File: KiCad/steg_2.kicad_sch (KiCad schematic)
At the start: 10 parts, among them U12 W65C02S

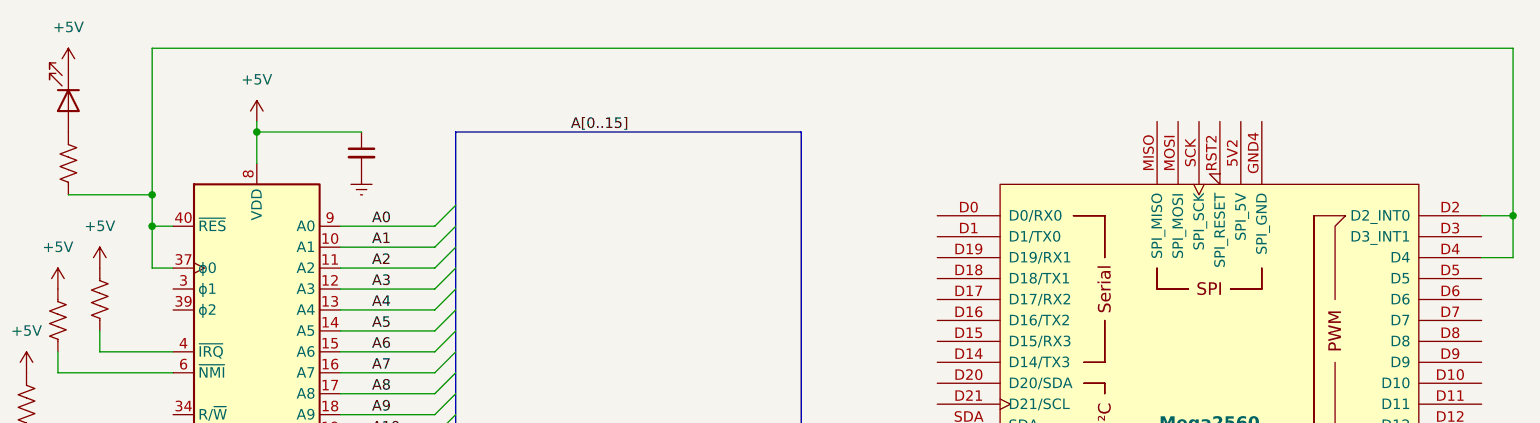
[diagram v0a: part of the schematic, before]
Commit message: Add trim potentiometer symbol and update power symbols in schematics
- Introduced a new trim potentiometer symbol (Device:R_Potentiometer_Trim) with properties for reference, value, footprint, and simulation details.
- Updated existing power symbols for +5V and Earth, including new references and descriptions.
- Adjusted positions and properties of various components in the schematic to enhance clarity and organization.
- Updated multiple schematic images to reflect the latest changes.
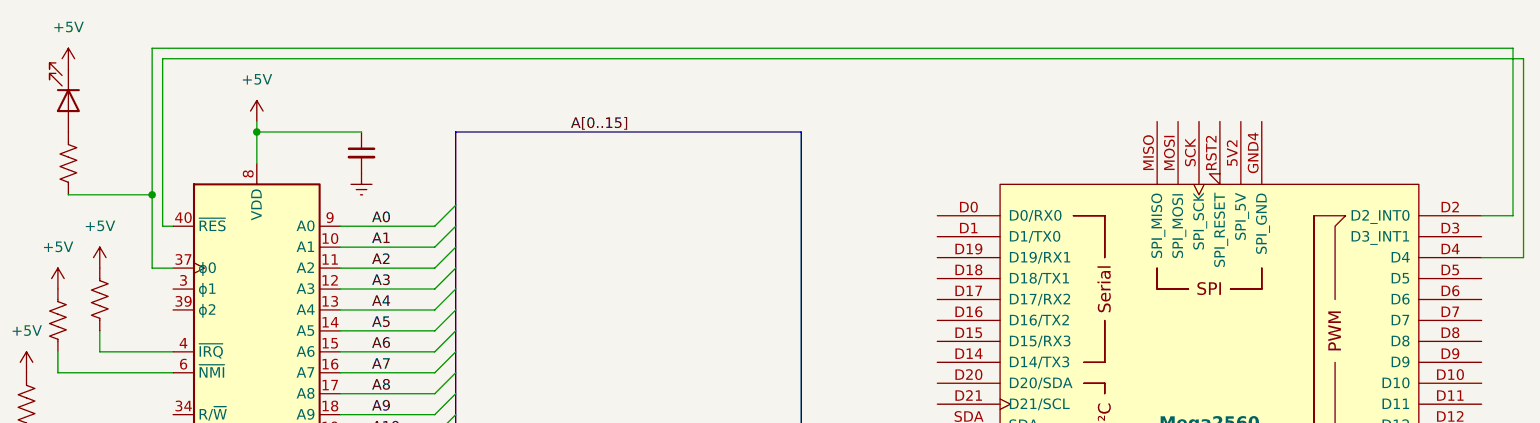
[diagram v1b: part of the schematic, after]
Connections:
- net at A6.D2 (D2_INT0), R34.2, U12.37 (ϕ0): no longer A6.D4, U12.40 (~{RES})
- new net: A6.D4, U12.40 (~{RES})
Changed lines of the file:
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@@
-	)
-	(junction
-		(at 259.08 67.31)
-		(diameter 0)
-		(color 0 0 0 0)
 	)
 	(junction
@@
 		(color 0 0 0 0)
 	)
-	(junction
-		(at 93.98 68.58)
-		(diameter 0)
-		(color 0 0 0 0)
-	)
 	(bus_entry
 		(at 172.72 128.27)
@@
 	(wire
 		(pts
-			(xy 93.98 68.58) (xy 93.98 73.66)
-		)
-		(stroke
-			(width 0)
-			(type default)
-		)
-	)
-	(wire
-		(pts
 			(xy 175.26 128.27) (xy 189.23 128.27)
 		)
@@
 	(wire
 		(pts
-			(xy 259.08 72.39) (xy 255.27 72.39)
-		)
-		(stroke
-			(width 0)
-			(type default)
-		)
-	)
-	(wire
-		(pts
 			(xy 116.84 104.14) (xy 128.27 104.14)
 		)
@@
 	(wire
 		(pts
-			(xy 96.52 68.58) (xy 93.98 68.58)
-		)
-		(stroke
-			(width 0)
-			(type default)
-		)
-	)
-	(wire
-		(pts
 			(xy 116.84 73.66) (xy 128.27 73.66)
 		)
@@
 	(wire
 		(pts
+			(xy 95.25 68.58) (xy 95.25 48.26)
+		)
+		(stroke
+			(width 0)
+			(type default)
+		)
+	)
+	(wire
+		(pts
 			(xy 106.68 57.15) (xy 106.68 60.96)
 		)
@@
 	(wire
 		(pts
-			(xy 93.98 64.77) (xy 93.98 68.58)
+			(xy 93.98 64.77) (xy 93.98 73.66)
 		)
 		(stroke
@@
 	(wire
 		(pts
+			(xy 255.27 72.39) (xy 260.35 72.39)
+		)
+		(stroke
+			(width 0)
+			(type default)
+		)
+	)
+	(wire
+		(pts
 			(xy 93.98 73.66) (xy 96.52 73.66)
 		)
@@
 	(wire
 		(pts
+			(xy 96.52 68.58) (xy 95.25 68.58)
+		)
+		(stroke
+			(width 0)
+			(type default)
+		)
+	)
+	(wire
+		(pts
 			(xy 259.08 46.99) (xy 259.08 67.31)
 		)
@@
 	(wire
 		(pts
+			(xy 95.25 48.26) (xy 260.35 48.26)
+		)
+		(stroke
+			(width 0)
+			(type default)
+		)
+	)
+	(wire
+		(pts
 			(xy 189.23 176.53) (xy 186.69 176.53)
 		)
@@
 	(wire
 		(pts
+			(xy 260.35 48.26) (xy 260.35 72.39)
+		)
+		(stroke
+			(width 0)
+			(type default)
+		)
+	)
+	(wire
+		(pts
 			(xy 116.84 83.82) (xy 128.27 83.82)
 		)
@@
 		)
 		(stroke
-			(width 0)
-			(type default)
-		)
-	)
-	(wire
-		(pts
-			(xy 259.08 67.31) (xy 259.08 72.39)
-		)
-		(stroke

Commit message: Revert "Add trim potentiometer symbol and update power symbols in schematics"
This reverts commit c4bb345892a428583a00d61d4c040ffcc3a1eb40.
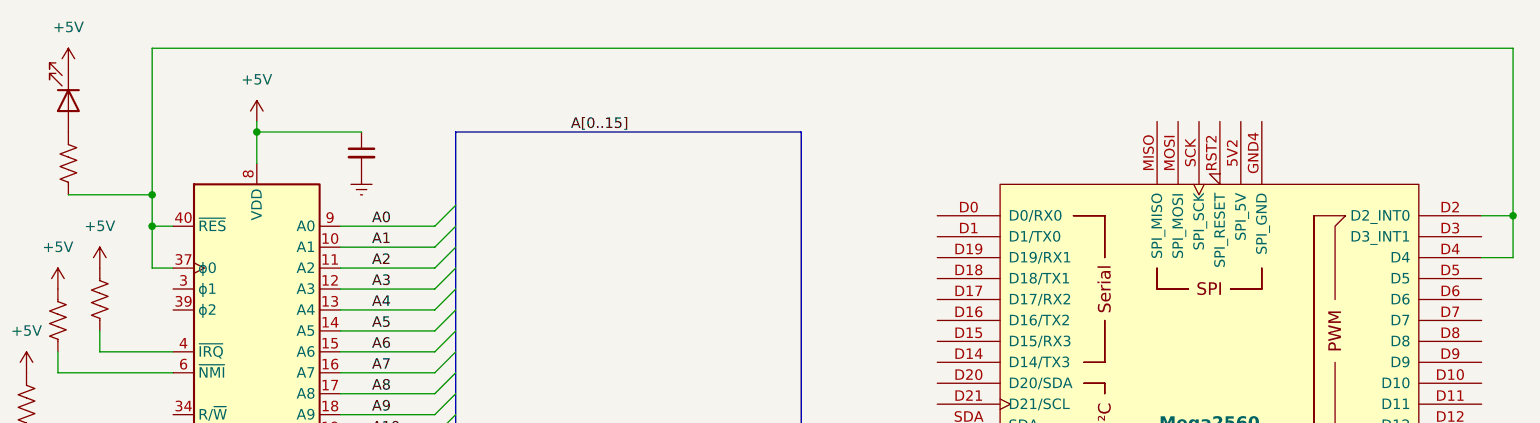
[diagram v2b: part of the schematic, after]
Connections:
- net at A6.D2 (D2_INT0), R34.2, U12.37 (ϕ0): now also A6.D4, U12.40 (~{RES})
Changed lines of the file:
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@@
+	)
+	(junction
+		(at 259.08 67.31)
+		(diameter 0)
+		(color 0 0 0 0)
 	)
 	(junction
@@
 		(color 0 0 0 0)
 	)
+	(junction
+		(at 93.98 68.58)
+		(diameter 0)
+		(color 0 0 0 0)
+	)
 	(bus_entry
 		(at 172.72 128.27)
@@
 	(wire
 		(pts
+			(xy 93.98 68.58) (xy 93.98 73.66)
+		)
+		(stroke
+			(width 0)
+			(type default)
+		)
+	)
+	(wire
+		(pts
 			(xy 175.26 128.27) (xy 189.23 128.27)
 		)
@@
 	(wire
 		(pts
+			(xy 259.08 72.39) (xy 255.27 72.39)
+		)
+		(stroke
+			(width 0)
+			(type default)
+		)
+	)
+	(wire
+		(pts
 			(xy 116.84 104.14) (xy 128.27 104.14)
 		)
@@
 	(wire
 		(pts
+			(xy 96.52 68.58) (xy 93.98 68.58)
+		)
+		(stroke
+			(width 0)
+			(type default)
+		)
+	)
+	(wire
+		(pts
 			(xy 116.84 73.66) (xy 128.27 73.66)
 		)
@@
 	(wire
 		(pts
-			(xy 95.25 68.58) (xy 95.25 48.26)
-		)
-		(stroke
-			(width 0)
-			(type default)
-		)
-	)
-	(wire
-		(pts
 			(xy 106.68 57.15) (xy 106.68 60.96)
 		)
@@
 	(wire
 		(pts
-			(xy 93.98 64.77) (xy 93.98 73.66)
+			(xy 93.98 64.77) (xy 93.98 68.58)
 		)
 		(stroke
@@
 	(wire
 		(pts
-			(xy 255.27 72.39) (xy 260.35 72.39)
-		)
-		(stroke
-			(width 0)
-			(type default)
-		)
-	)
-	(wire
-		(pts
 			(xy 93.98 73.66) (xy 96.52 73.66)
 		)
@@
 	(wire
 		(pts
-			(xy 96.52 68.58) (xy 95.25 68.58)
-		)
-		(stroke
-			(width 0)
-			(type default)
-		)
-	)
-	(wire
-		(pts
 			(xy 259.08 46.99) (xy 259.08 67.31)
 		)
@@
 	(wire
 		(pts
-			(xy 95.25 48.26) (xy 260.35 48.26)
-		)
-		(stroke
-			(width 0)
-			(type default)
-		)
-	)
-	(wire
-		(pts
 			(xy 189.23 176.53) (xy 186.69 176.53)
 		)
@@
 	(wire
 		(pts
-			(xy 260.35 48.26) (xy 260.35 72.39)
-		)
-		(stroke
-			(width 0)
-			(type default)
-		)
-	)
-	(wire
-		(pts
 			(xy 116.84 83.82) (xy 128.27 83.82)
 		)
@@
 		)
 		(stroke
+			(width 0)
+			(type default)
+		)
+	)
+	(wire
+		(pts
+			(xy 259.08 67.31) (xy 259.08 72.39)
+		)
+		(stroke
